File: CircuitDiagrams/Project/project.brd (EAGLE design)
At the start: 100 x 70 mm, 124 parts, among them IC1 UC3C, IC2 PCA9542A, IC3 MT48LC4M16A2TSOP54, IC4 TB6593FNGSSOP20, IC5 TB6593FNGSSOP20, J1 JTAG2.54MM2X5TH, J2 1BY2THROUGHHOLE, J3 1BY2THROUGHHOLE, J4 1BY2THROUGHHOLE, J5 8PIN2.54MM2X4TH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

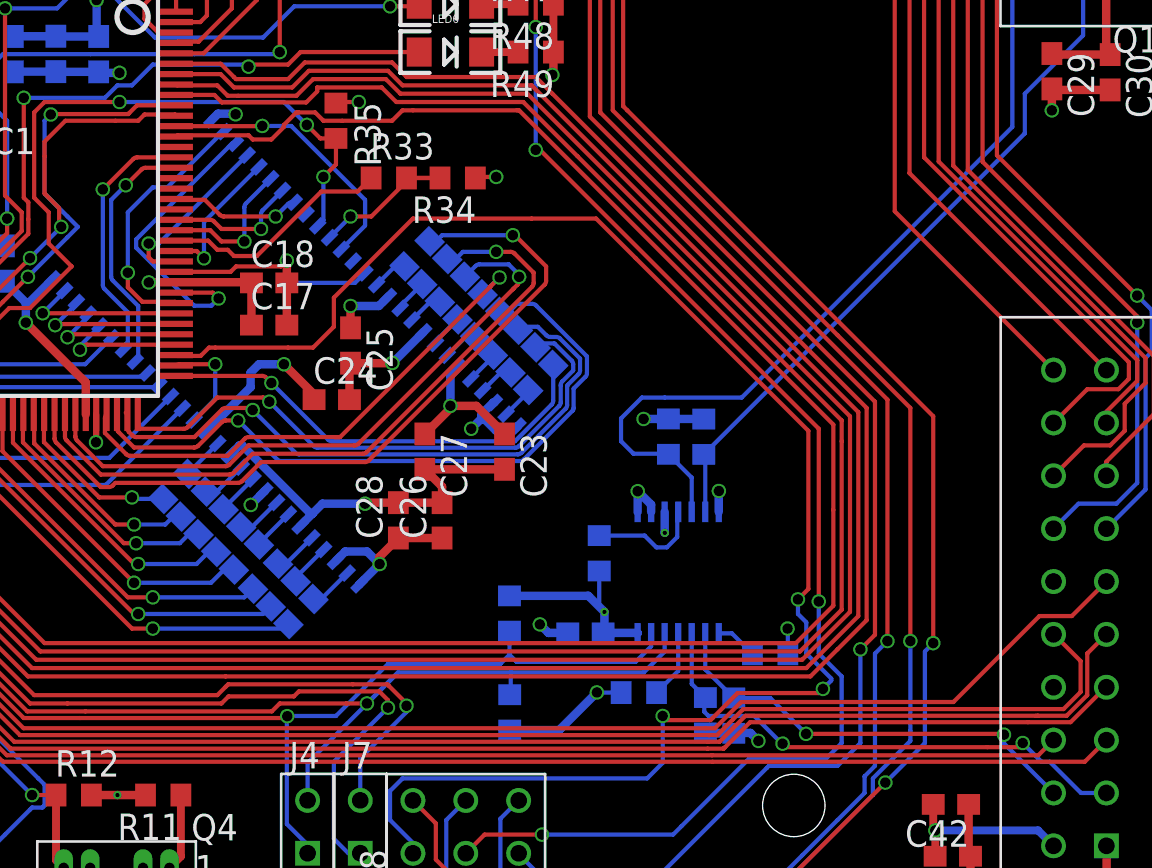
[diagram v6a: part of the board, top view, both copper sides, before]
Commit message: Corrected all keepout errors!
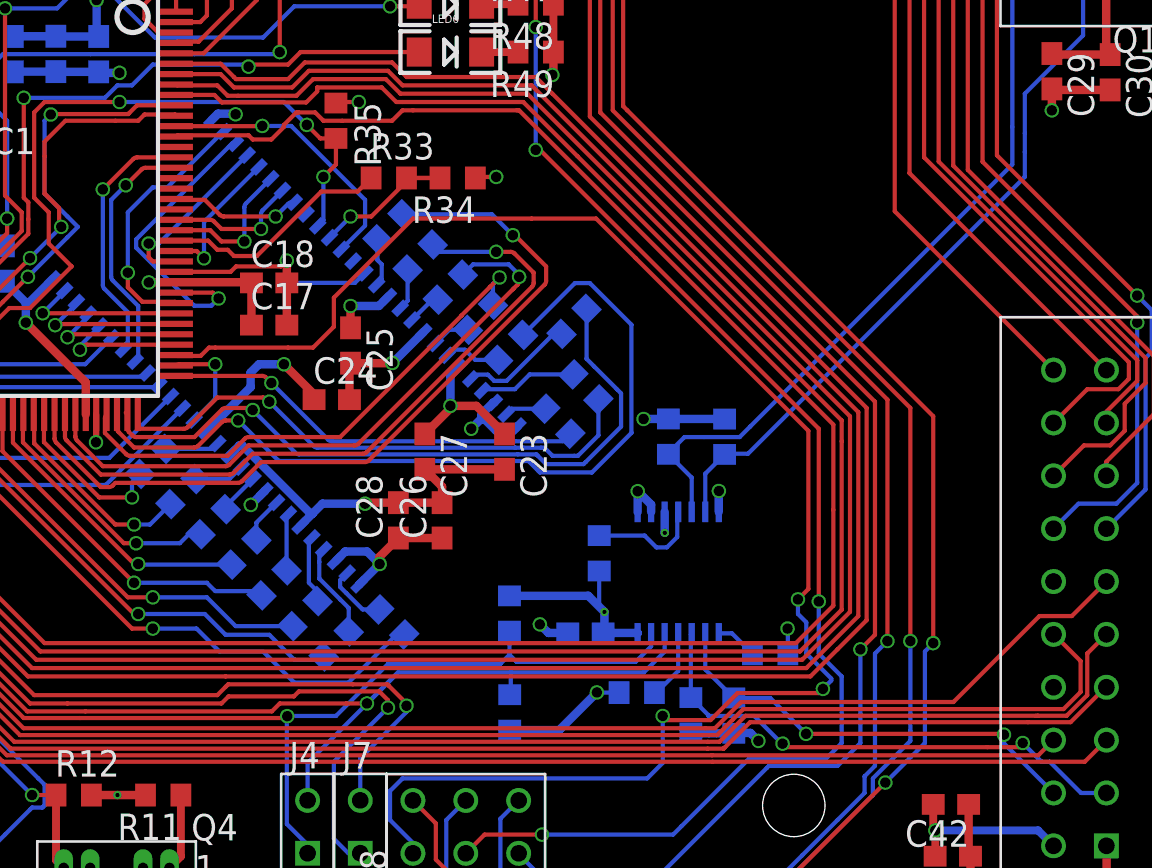
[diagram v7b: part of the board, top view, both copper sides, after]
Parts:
- moved R17 4.39 mm to (62.7, 13.8), turned to 225 degrees
- moved R18 3.51 mm to (60.0, 12.8)
- moved R30 3.45 mm to (71.4, 28.3)
- moved R31 3.29 mm to (72.0, 25.1), turned to 225 degrees
- moved R19 2.62 mm to (58.5, 14.2)
- moved R32 2.26 mm to (70.7, 23.5), turned to 225 degrees
- moved R25 1.84 mm to (62.6, 32.8)
- moved R20 1.82 mm to (57.0, 15.7)
- moved R24 1.63 mm to (51.2, 21.5)
- moved R29 1.56 mm to (68.4, 27.0)
- moved R8 1.00 mm to (78.7, 22.7)
- moved R26 0.99 mm to (64.0, 31.4)
- moved R21 0.95 mm to (55.6, 17.2)
- moved R23 0.78 mm to (52.7, 20.1)
- moved R28 0.71 mm to (66.9, 28.5)
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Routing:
- net PC19: track 21.1 -> 28.6 mm
- net PC31: track 33.7 -> 40.4 mm
- net SDA0: track 42.2 -> 38.1 mm
- net DQ13: track 1.60 -> 5.50 mm
- net PC20: track 19.3 -> 22.7 mm
- net DQ14: track 1.71 -> 4.69 mm
- net PD0: track 30.7 -> 33.4 mm
- net DQ01: track 2.08 -> 4.61 mm
- net PC21: track 17.7 -> 20.0 mm
- net PD1: track 28.3 -> 26.7 mm
- net PC27: track 36.9 -> 38.5 mm
- net PD2: track 22.0 -> 20.4 mm
- net PC22: track 15.8 -> 17.1 mm
- net DQ02: track 2.14 -> 3.27 mm
- net DQ12: track 1.71 -> 2.76 mm
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
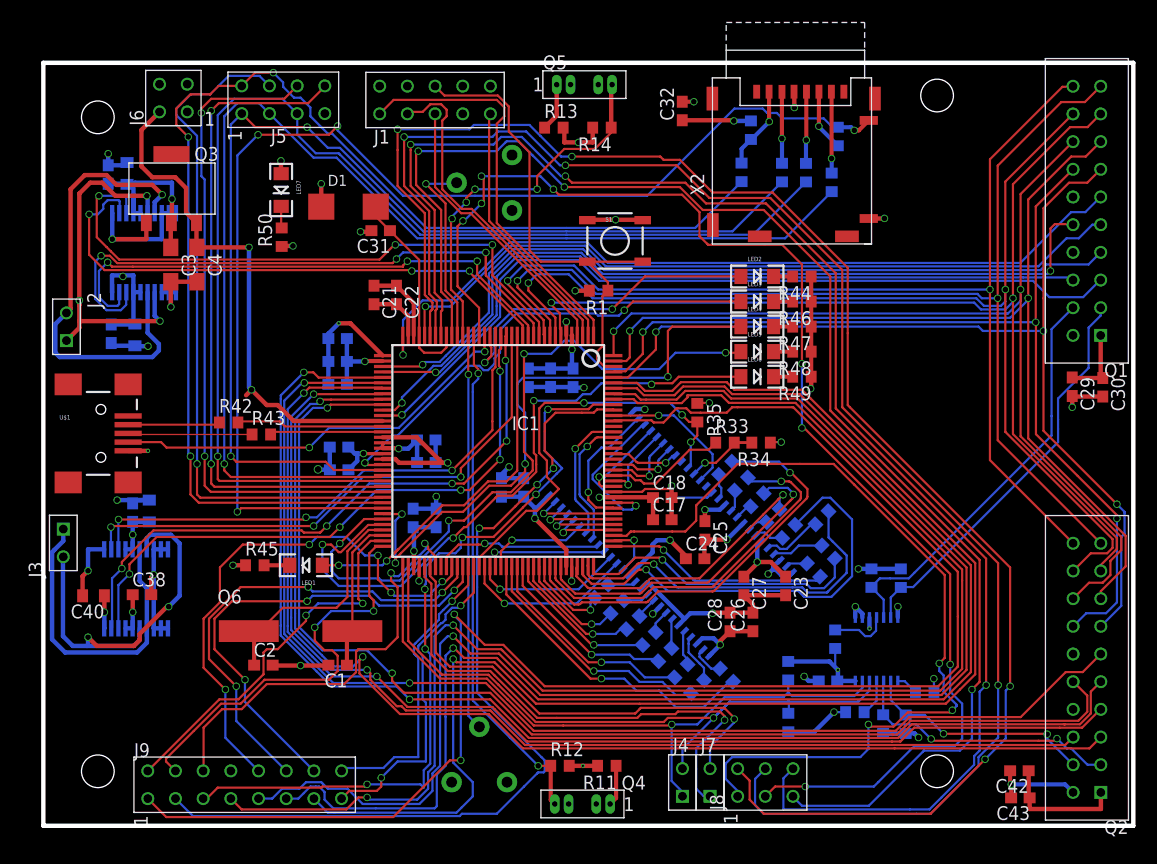
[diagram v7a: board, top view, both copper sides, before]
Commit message: Changed some minor things on the PCB
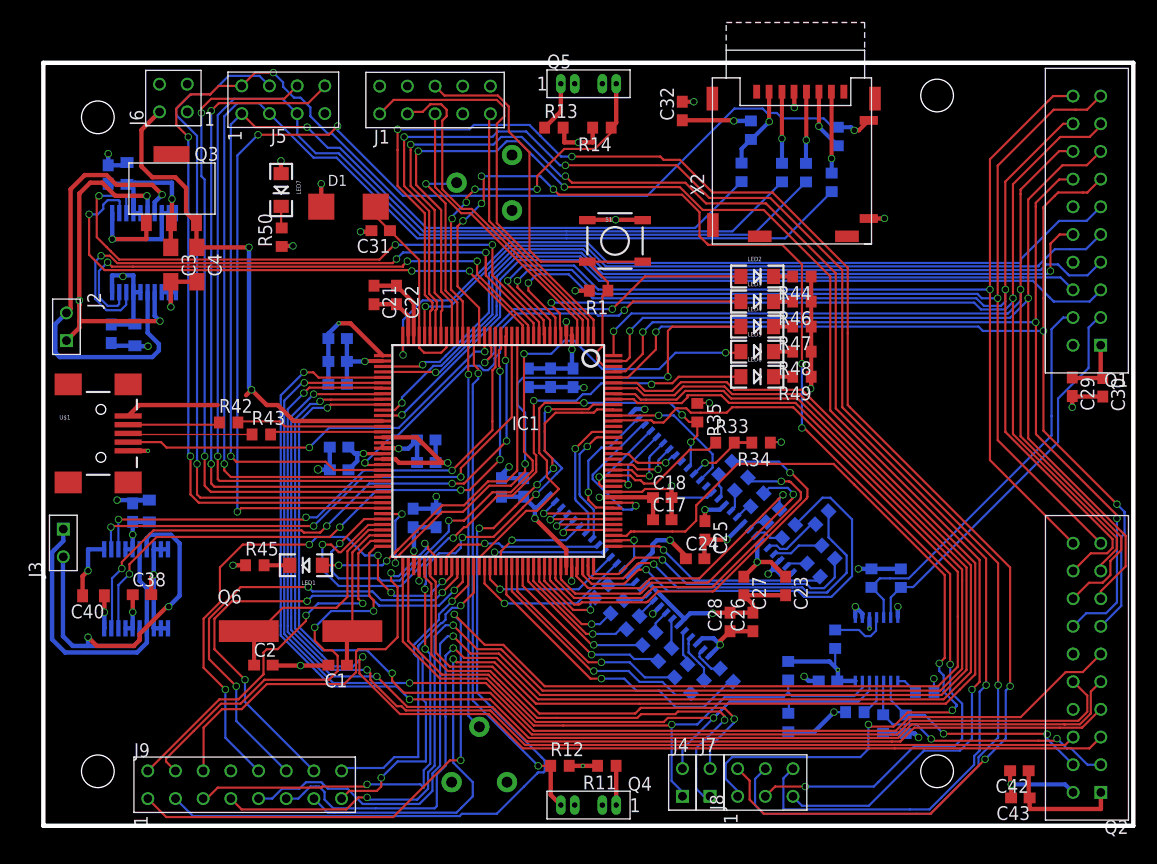
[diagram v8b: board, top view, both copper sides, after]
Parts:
- moved Q1 0.90 mm to (97.0, 44.1)
- moved Q4 0.57 mm to (52.6, 1.90)
- moved Q5 0.39 mm to (47.5, 68.1)
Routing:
- net +5V: track 48.3 -> 57.0 mm
- net PA28: track 76.7 -> 75.5 mm
- net +3V3: track 182.0 -> 181.1 mm
- net SCL0: track 37.2 -> 36.4 mm
